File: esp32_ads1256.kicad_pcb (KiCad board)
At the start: 2 copper layers, 70 x 75 mm, 72 parts, among them J1 uart, J2 Conn_01x02, J4 i2c, U1 ADS1256IDBR, U2 OPA2727AID, U3 OPA2727AID, U4 OPA2727AID, U5 OPA2727AID, U6 OPA350UA, U7 ESP32-S3-DEVKITC-1-N8R2, Y1 Crystal

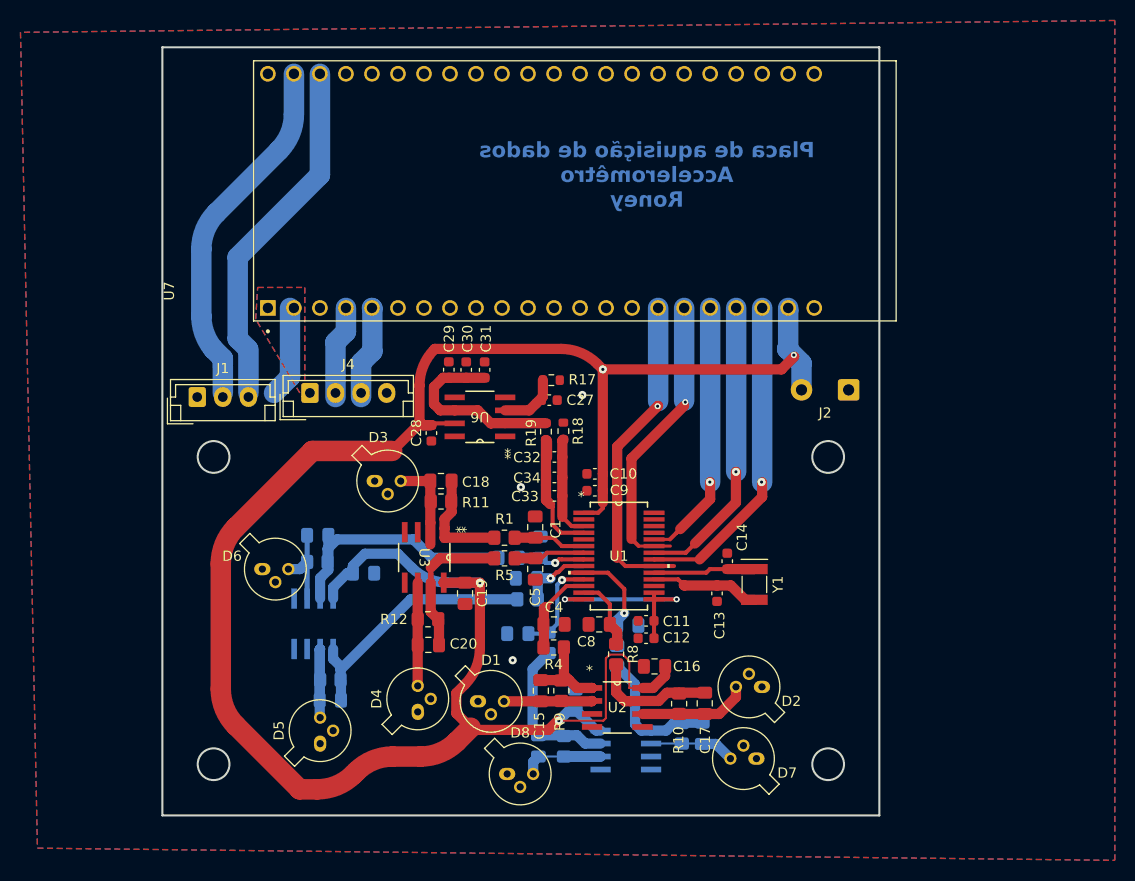
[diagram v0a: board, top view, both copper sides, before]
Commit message: substituição do buffer de tensão com opa350 pela referencia de tensão ADR441xRZ
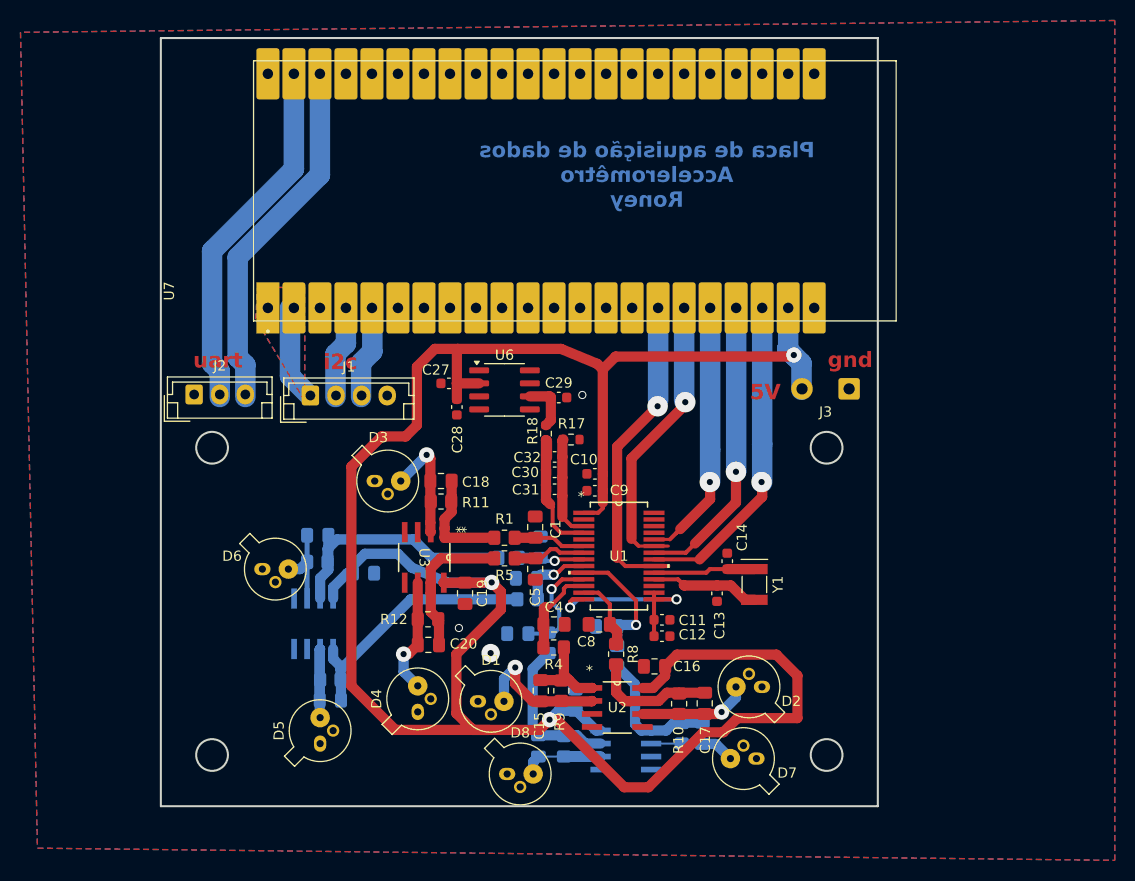
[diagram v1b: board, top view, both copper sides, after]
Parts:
- removed C33: 0.1uF, Capacitor_SMD:C_0603_1608Metric
- removed C34: 100pF, Capacitor_SMD:C_0603_1608Metric
- removed J4: i2c, Connector_JST:JST_EH_B4B-EH-A_1x04_P2.50mm_Vertical
- removed R19: 49.9, Resistor_SMD:R_0603_1608Metric
- added J3: Conn_01x02, Connector_Wire:SolderWire-0.5sqmm_1x02_P4.6mm_D0.9mm_OD2.1mm, F.Cu at (121.0, 86.9)
- C13, C14: value 10pF -> 18pF
- C27: value 1uF -> 47uF
- C29: value 47uF -> 0.1uF
- C30: value 0.1uF -> 47uF
- C31: value 100uF -> 0.1uF
- C32: value 47uF -> 100pF
- J1: value uart -> i2c; footprint Connector_JST:JST_EH_B3B-EH-A_1x03_P2.50mm_Vertical -> Connector_JST:JST_EH_B4B-EH-A_1x04_P2.50mm_Vertical
- J2: value Conn_01x02 -> uart; footprint Connector_Wire:SolderWire-0.5sqmm_1x02_P4.6mm_D0.9mm_OD2.1mm -> Connector_JST:JST_EH_B3B-EH-A_1x03_P2.50mm_Vertical
- R17: value 10k -> 49.9
- U6: value OPA350UA -> ADR441xRZ; footprint local:opa350ua_D8 -> Package_SO:SOIC-8_3.9x4.9mm_P1.27mm
- moved J2 63.9 mm to (57.1, 87.5), turned to 0 degrees
- moved C31 13.5 mm to (92.3, 96.7), turned to 180 degrees
- moved C30 13.2 mm to (92.3, 95.0), turned to 180 degrees
- moved C29 11.1 mm to (92.7, 87.8), turned to 0 degrees
- moved J1 11.1 mm to (68.5, 87.5)
- moved C27 9.94 mm to (82.0, 86.4)
- moved R17 6.11 mm to (93.9, 91.8), turned to 180 degrees
- moved U6 3.56 mm to (87.4, 87.0), turned to 0 degrees
- moved C28 3.56 mm to (82.8, 88.7)
- moved C3 2.08 mm to (97.4, 110.1), turned to 180 degrees
- moved R18 1.72 mm to (91.5, 91.3)
- moved C12 1.56 mm to (102.8, 111.0), turned to 0 degrees
- moved C11 1.55 mm to (102.8, 109.5), turned to 0 degrees
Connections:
- C27 pad 1: GND -> +5V
- C27 pad 2: Net-(U6-IN+) -> GND
- C29 pad 1: Net-(U6-IN-) -> Net-(U6-V_{OUT})
- C30 pad 1: Net-(U6-IN-) -> /reference_voltage/vrefn
- C30 pad 2: GND -> /reference_voltage/vrefp
- C31 pad 1: Net-(U6-IN-) -> /reference_voltage/vrefn
- C31 pad 2: GND -> /reference_voltage/vrefp
- C32 pad 1: /voltage_reference_buffer/vrefn -> /reference_voltage/vrefn
- C32 pad 2: /voltage_reference_buffer/vrefp -> /reference_voltage/vrefp
- J1 pad 1: GND -> +3.3V
- J1 pad 2: /microcontroler/tx1 -> Net-(J1-Pin_2)
- J1 pad 3: /microcontroler/rx1 -> Net-(J1-Pin_3)
- J2 pad 2: +5V -> /microcontroler/tx1
- R17 pad 1: Net-(U6-IN+) -> GND
- R17 pad 2: +2V5 -> /reference_voltage/vrefn
- R18 pad 1: GND -> Net-(U6-V_{OUT})
- R18 pad 2: /voltage_reference_buffer/vrefn -> /reference_voltage/vrefp
- U1 pad 3: /voltage_reference_buffer/vrefn -> /reference_voltage/vrefn
- U1 pad 4: /voltage_reference_buffer/vrefp -> /reference_voltage/vrefp
- U6 pad 2: Net-(U6-IN-) -> +5V
- U6 pad 3: Net-(U6-IN+) -> unconnected-(U6-NC-Pad3)
- U6 pad 6: Net-(U6-IN-) -> Net-(U6-V_{OUT})
- U6 pad 7: +5V -> unconnected-(U6-NC-Pad7)
- U7 pad J1_4: Net-(J4-Pin_2) -> Net-(J1-Pin_2)
- U7 pad J1_5: Net-(J4-Pin_3) -> Net-(J1-Pin_3)
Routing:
- net Net-(U6-IN-): track 18.7 -> 0.00 mm
- net /voltage_reference_buffer/vrefp: track 15.7 -> 0.00 mm
- net /reference_voltage/vrefp: track 0.00 -> 15.7 mm
- net +5V: track 214.8 -> 228.4 mm, vias 4 -> 3
- net /voltage_reference_buffer/vrefn: track 10.1 -> 0.00 mm
- net /reference_voltage/vrefn: track 0.00 -> 10.1 mm
- net Net-(J4-Pin_3): track 9.17 -> 0.00 mm
- net Net-(J1-Pin_3): track 0.00 -> 9.17 mm
- net Net-(J4-Pin_2): track 9.12 -> 0.00 mm
- net Net-(J1-Pin_2): track 0.00 -> 9.12 mm
- net Net-(U6-IN+): track 6.51 -> 0.00 mm
- net Net-(U6-V_{OUT}): track 0.00 -> 4.99 mm
- net Net-(D1-K): track 8.66 -> 13.6 mm, vias 0 -> 1
- net /microcontroler/int_bar: track 31.5 -> 35.3 mm
- net /microcontroler/sclk: track 26.6 -> 29.8 mm
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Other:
- outline, holes or cut-outs redrawn
- board text added: "5V"
- board text added: "gnd"
- board text added: "i2c"
- board text added: "uart"
